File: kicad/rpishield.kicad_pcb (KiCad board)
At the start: 2 copper layers, 64 x 56 mm, 23 parts

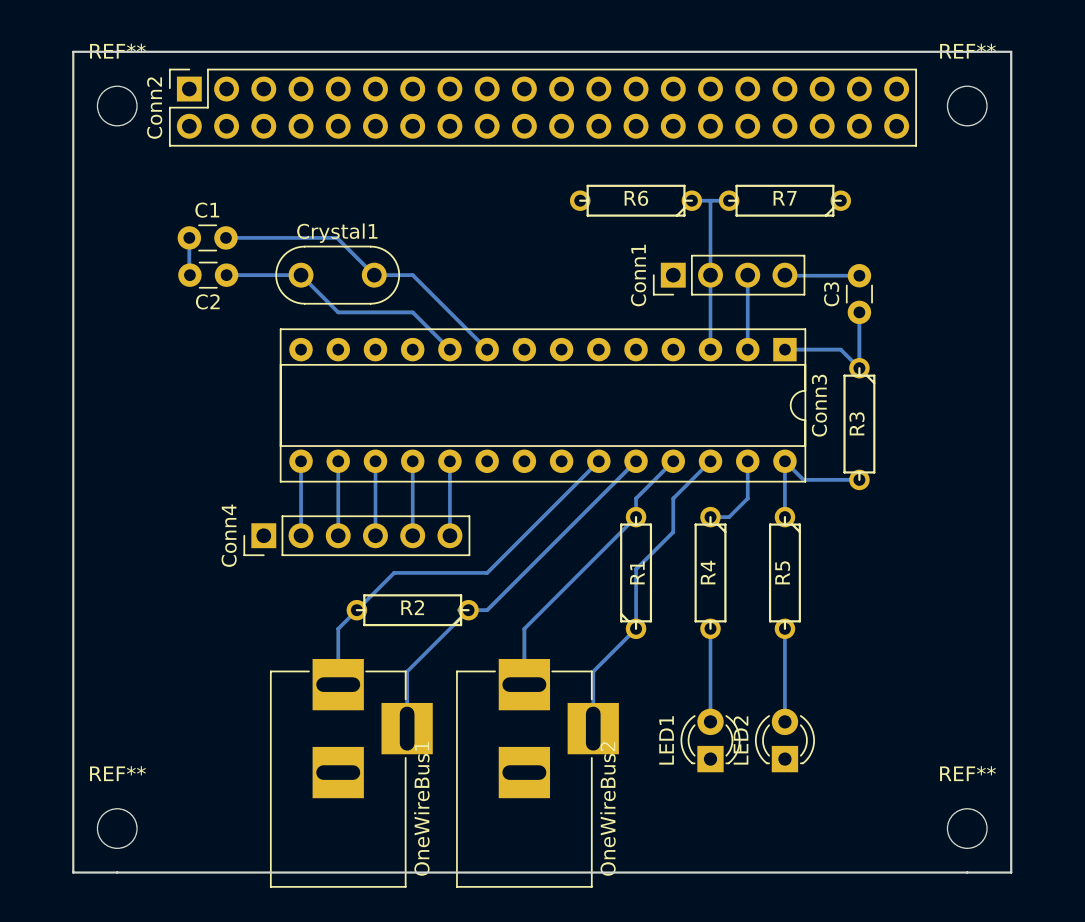
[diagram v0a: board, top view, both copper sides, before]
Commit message: Round corner, via, gnd pour.
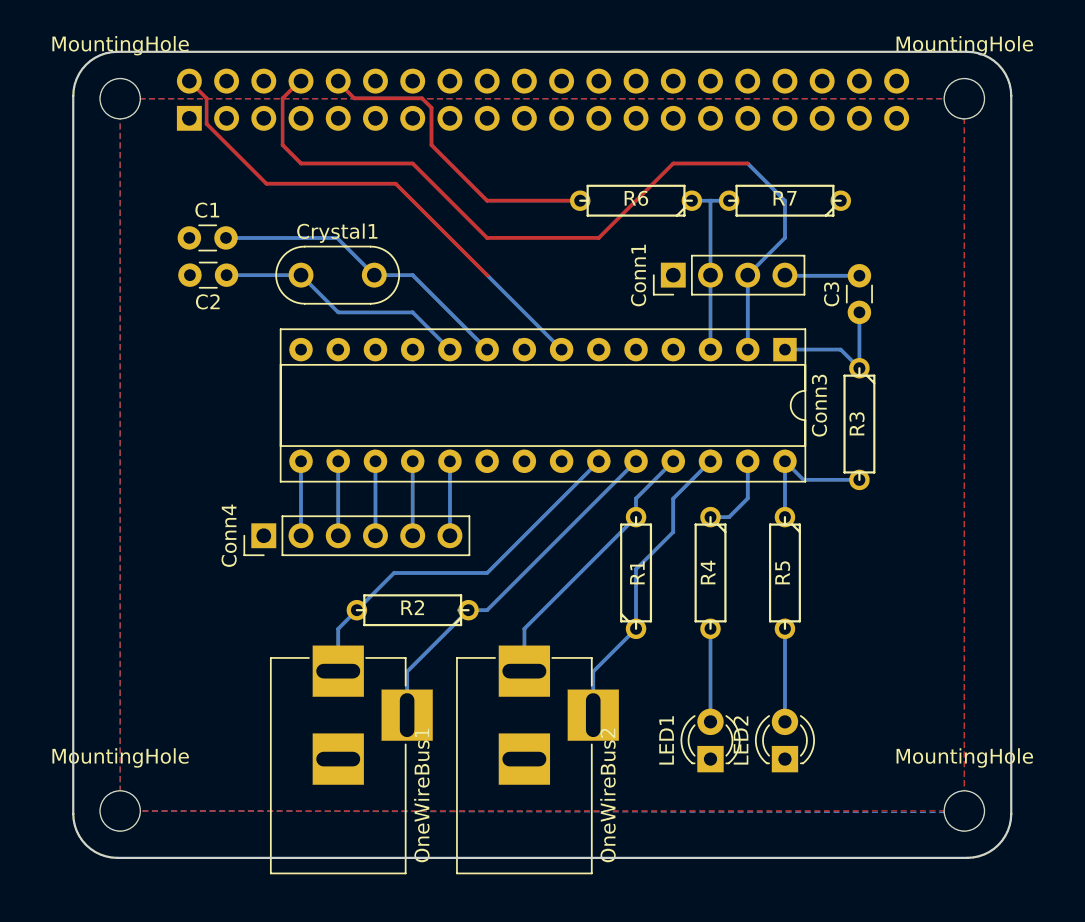
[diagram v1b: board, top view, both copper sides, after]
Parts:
- Conn2: moved to B.Cu
- MountingHole (x4): renamed from REF**; value MountingHole_2.7mm_M2.5 -> MountingHole_2.75mm_M2.5
- moved Conn2 2.00 mm to (121.9, 68.0), turned to 270 degrees
- moved MountingHole 1.22 mm to (117.2, 115.3)
- moved MountingHole 1.22 mm to (174.8, 115.3)
- moved OneWireBus1 0.92 mm to (132.1, 105.8)
- moved OneWireBus2 0.92 mm to (144.8, 105.8)
- moved MountingHole 0.54 mm to (117.2, 66.7)
- moved MountingHole 0.54 mm to (174.8, 66.7)
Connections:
- Conn2 pad 1: /VCC -> Net-(Conn2-Pad1)
- Conn2 pad 10: GND -> /RX_RPI
- Conn2 pad 2: Net-(Conn2-Pad2) -> /VCC
- Conn2 pad 25: Net-(Conn2-Pad25) -> GND
- Conn2 pad 39: Net-(Conn2-Pad39) -> GND
- Conn2 pad 7: /RX -> Net-(Conn2-Pad7)
- Conn2 pad 8: Net-(Conn2-Pad8) -> /RX
- Conn2 pad 9: /RX_RPI -> GND
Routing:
- net /RX: track 5.62 -> 56.7 mm
- net /VCC: track 0.00 -> 34.0 mm
- net /RX_RPI: track 0.00 -> 21.5 mm
- net GND: track 3.28 -> 0.73 mm
- added copper zone on B.Cu, net GND
- added copper zone on F.Cu, net GND
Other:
- board size 64 x 56 mm -> 64 x 55 mm

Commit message: 20x2 pin strip.
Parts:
- Conn2: footprint Socket_Strips:Socket_Strip_Straight_2x20_Pitch2.54mm -> Pin_Headers:Pin_Header_Straight_2x20_Pitch2.54mm; moved to F.Cu
- moved Conn2 0.54 mm to (121.9, 68.6), turned to 90 degrees
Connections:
- net /VCC renamed /VCC_AVR
- Conn2 pad 1: Net-(Conn2-Pad1) -> /VCC_SPI
- Conn2 pad 10: /RX_RPI -> Net-(Conn2-Pad10)
- Conn2 pad 25: GND -> Net-(Conn2-Pad25)
- Conn2 pad 6: Net-(Conn2-Pad6) -> /RX
- Conn2 pad 8: /RX -> /RX_RPI
- Conn3 pad 15: /D9 -> Net-(Conn3-Pad15)
- Conn4 pad 2: /D9 -> /VCC_SPI
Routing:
- net /VCC_SPI: track 0.00 -> 33.2 mm
- net /D9: track 5.08 -> 0.00 mm
- net /RX_RPI: track 21.5 -> 24.4 mm
- net /RX: track 56.7 -> 54.5 mm
- net /VCC_AVR: track 34.0 -> 35.3 mm
- net GND: track 0.73 -> 0.00 mm
- removed copper zone on F.Cu, net GND

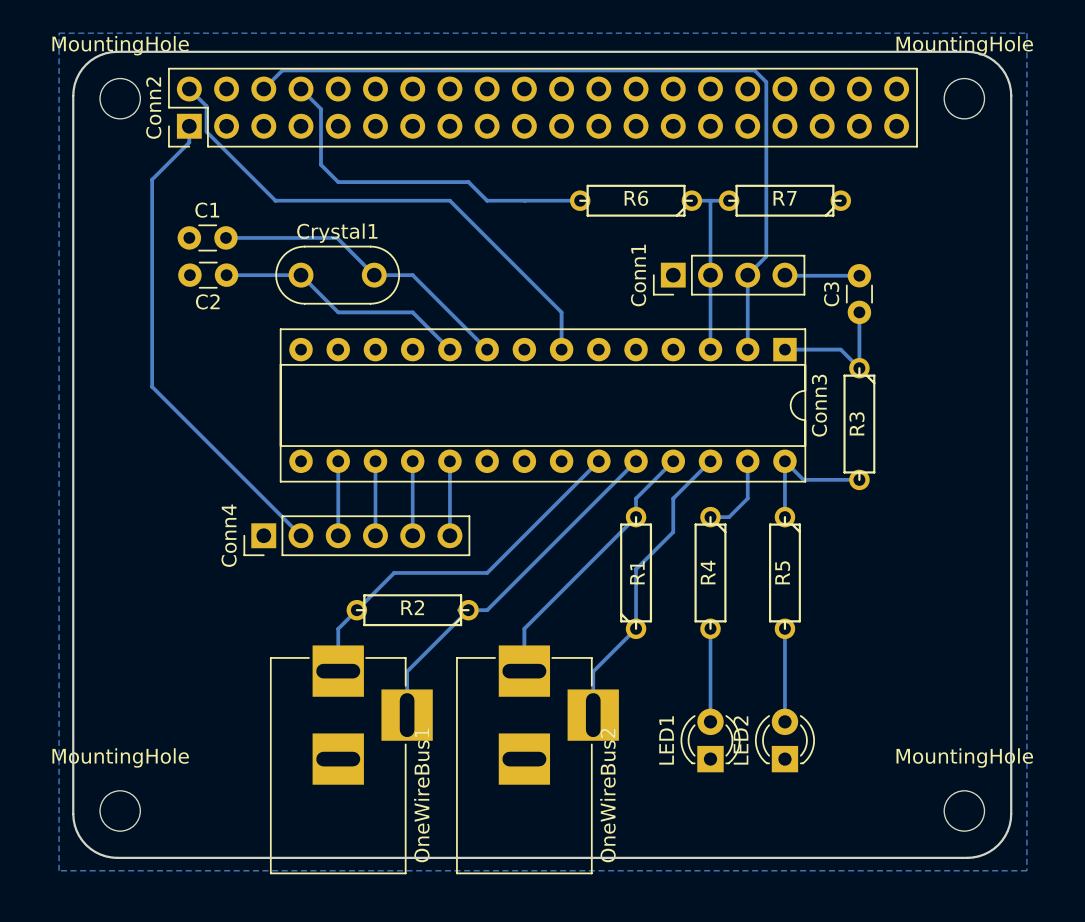
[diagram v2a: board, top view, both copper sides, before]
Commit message: Distance rule, custom header.
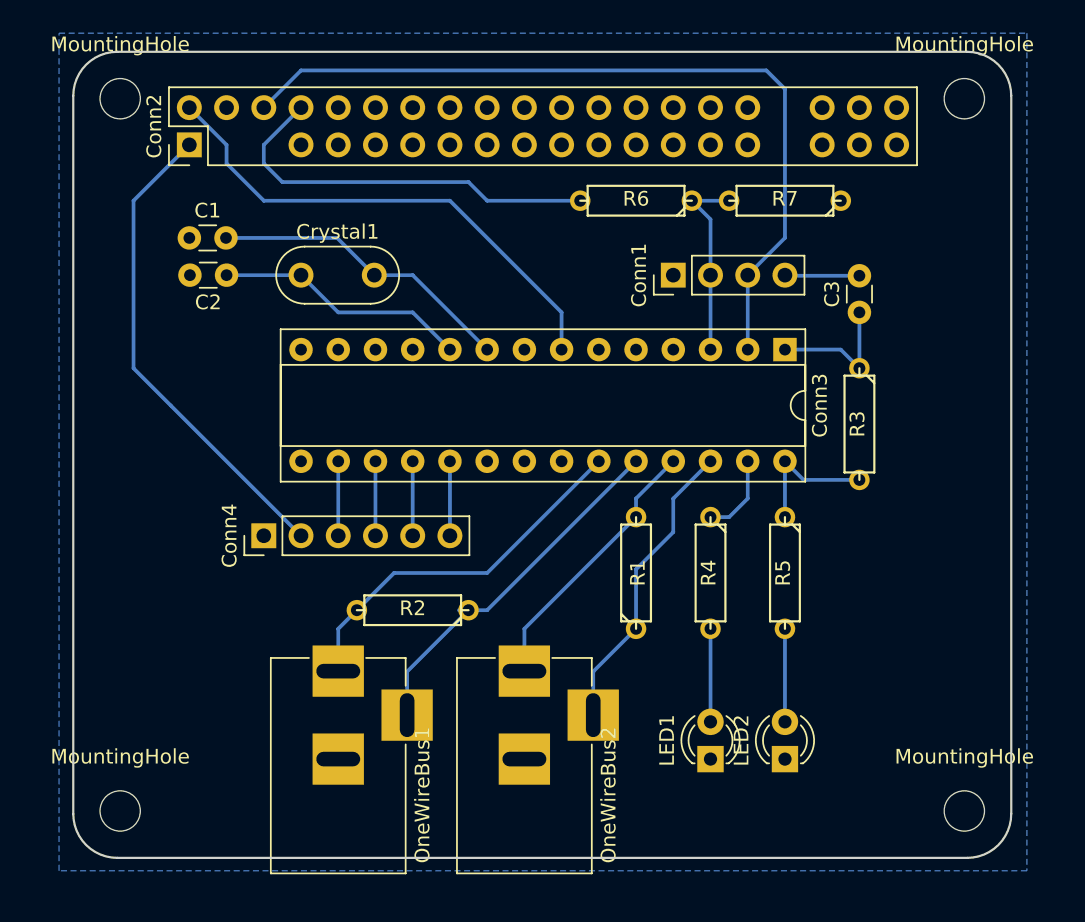
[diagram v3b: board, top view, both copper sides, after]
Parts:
- Conn2: footprint Pin_Headers:Pin_Header_Straight_2x20_Pitch2.54mm -> header220:Custom_Header_2x20_Pitch2.54mm
- moved Conn2 1.27 mm to (121.9, 69.8)
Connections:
- C1 pad 1: GND -> Net-(C1-Pad1)
- C2 pad 2: GND -> Net-(C1-Pad1)
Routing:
- net /RX_RPI: track 24.4 -> 27.5 mm
- net /RX: track 54.5 -> 56.5 mm
- net /VCC_AVR: track 35.3 -> 34.5 mm
- net /TX: track 13.2 -> 13.8 mm
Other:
- net class Default: clearance 0.2 -> 0.3
- rule pad_to_mask_clearance: 0.2 -> 0.3
- rule trace_clearance: 0.2 -> 0.3

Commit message: Ground fill, RPi pinhole, schema lib, cleanup.
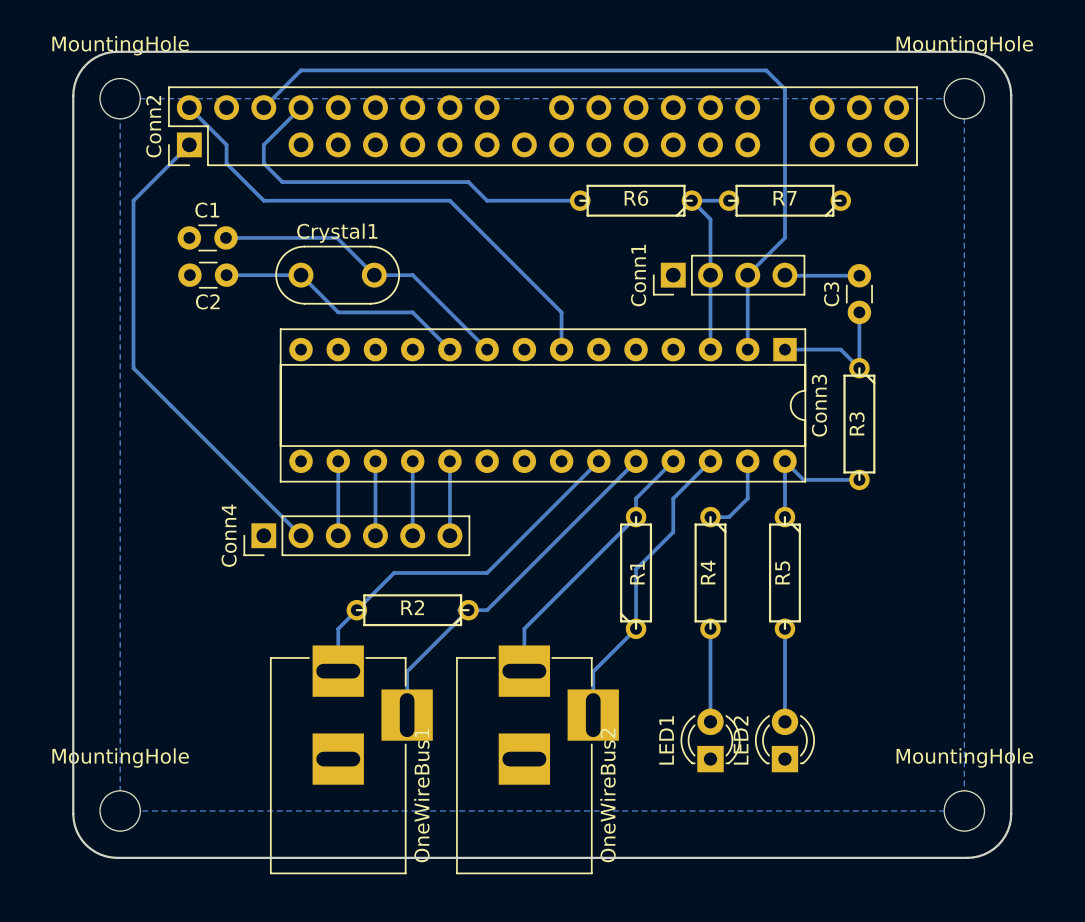
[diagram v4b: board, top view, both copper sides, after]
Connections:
- C1 pad 1: Net-(C1-Pad1) -> GND
- C2 pad 2: Net-(C1-Pad1) -> GND
- Conn2 pad 25: Net-(Conn2-Pad25) -> GND
- Conn2 pad 9: GND -> Net-(Conn2-Pad9)
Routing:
- net /RX: track 56.5 -> 56.0 mm

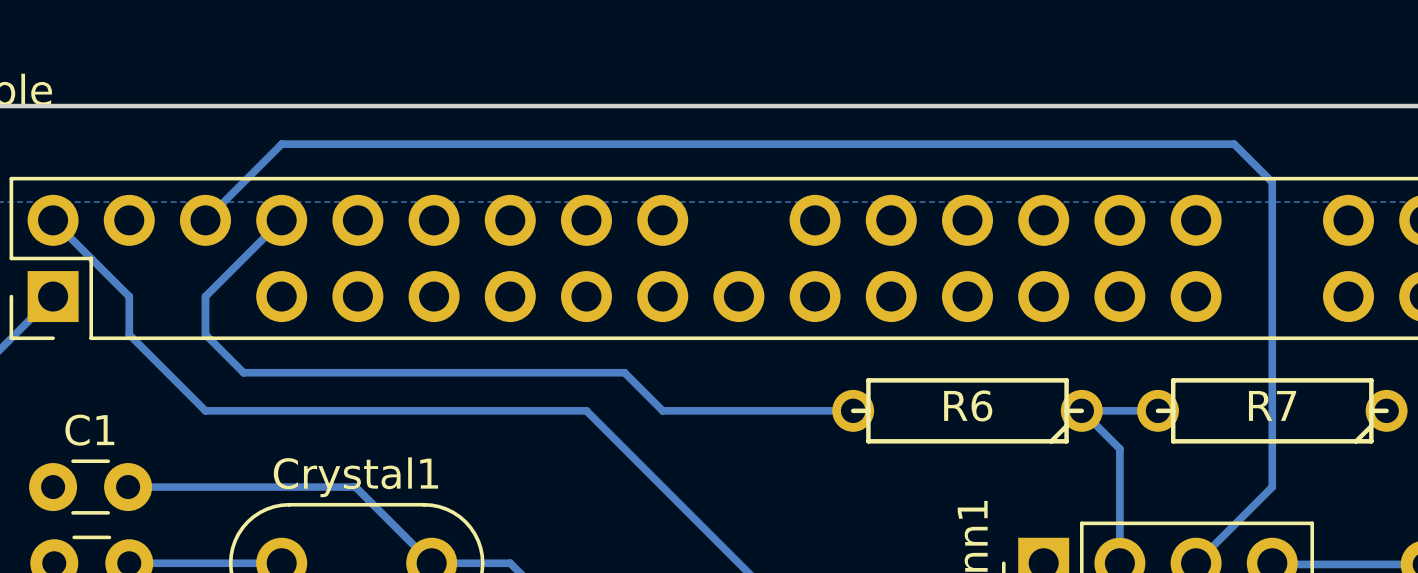
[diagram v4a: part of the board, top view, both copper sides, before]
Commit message: Obsolate models, RX/RT fix.
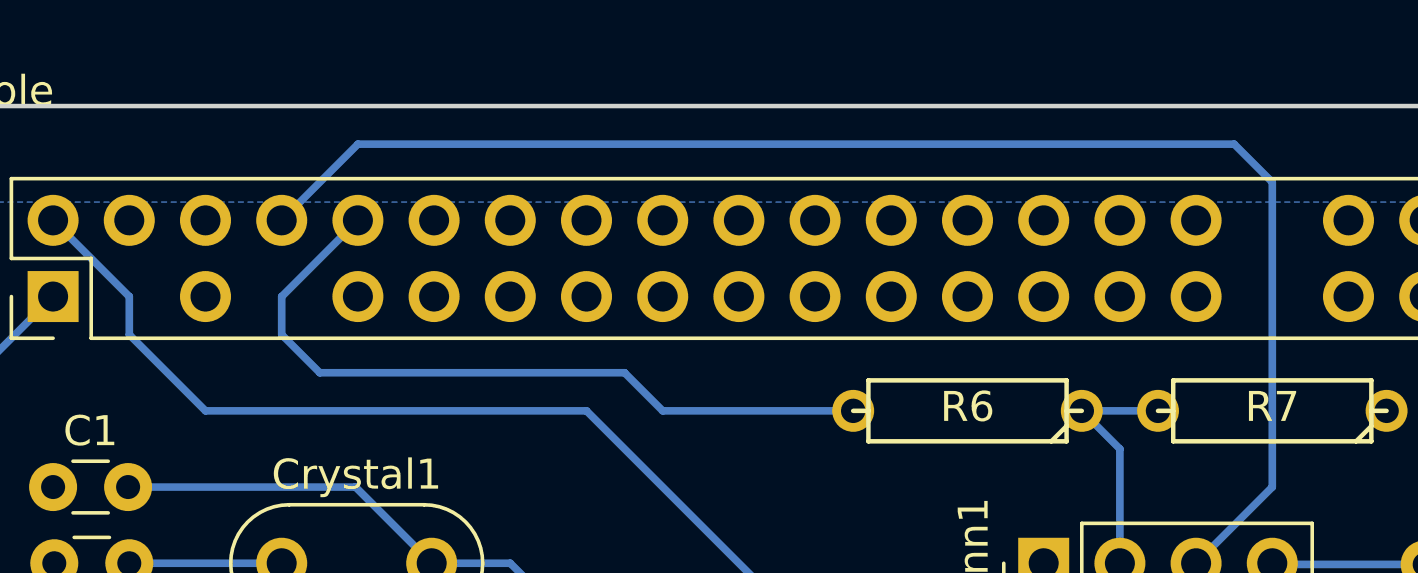
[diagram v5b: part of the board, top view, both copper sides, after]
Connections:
- Conn2 pad 10: Net-(Conn2-Pad10) -> /RX_RPI
- Conn2 pad 6: /RX -> Net-(Conn2-Pad6)
- Conn2 pad 8: /RX_RPI -> /RX
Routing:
- net /RX: track 56.0 -> 53.4 mm
- net /RX_RPI: track 27.5 -> 25.0 mm

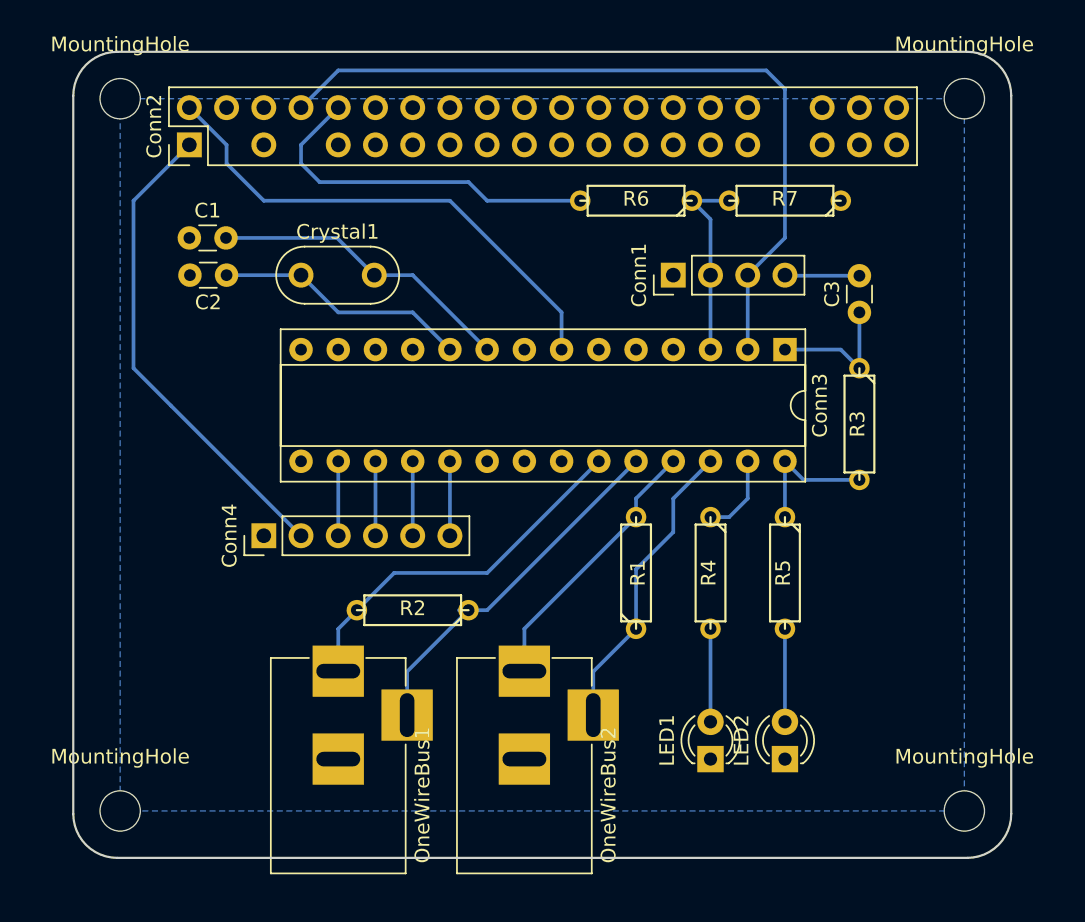
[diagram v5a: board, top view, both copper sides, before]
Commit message: Ground pad, track cleanup.
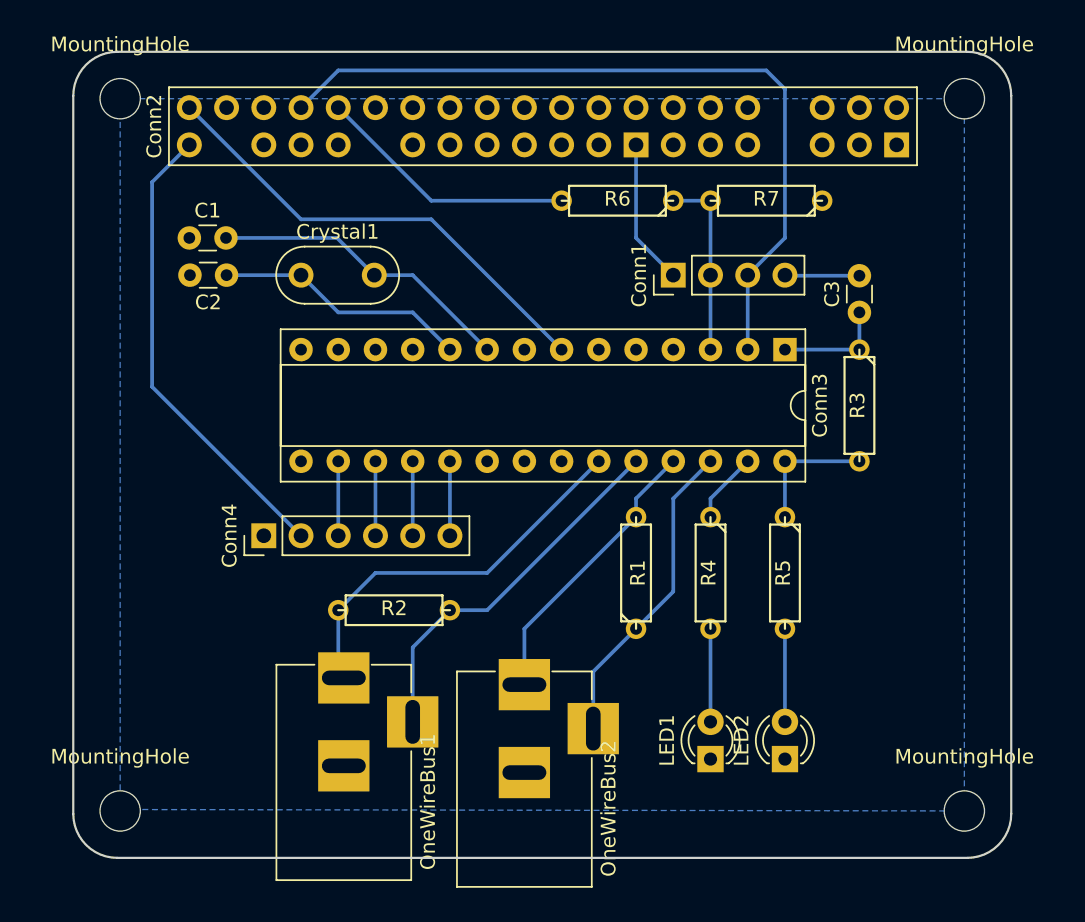
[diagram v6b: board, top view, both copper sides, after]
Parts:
- moved R2 1.27 mm to (135.9, 101.6)
- moved R3 1.27 mm to (167.6, 87.6)
- moved R6 1.27 mm to (151.1, 73.7)
- moved R7 1.27 mm to (161.3, 73.7)
- moved OneWireBus2 0.92 mm to (144.8, 106.7)
- moved OneWireBus1 0.60 mm to (132.5, 106.2)
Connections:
- Conn1 pad 1: GND -> /GND_UART
- Conn2 pad 25: GND -> /GND_UART
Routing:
- net /GND_UART: track 0.00 -> 9.94 mm
- net /RX_RPI: track 25.0 -> 17.9 mm
- net /VCC_AVR: track 34.5 -> 32.2 mm
- net /RST: track 9.68 -> 7.62 mm
- net /A5: track 10.0 -> 8.89 mm
- net /A4: track 5.99 -> 4.86 mm
- net /TX: track 13.8 -> 12.7 mm
- net /VCC_SPI: track 33.0 -> 31.9 mm
- net /A1: track 26.5 -> 25.6 mm
- net /XTAL1: track 21.6 -> 21.0 mm
- net /A2: track 20.0 -> 19.4 mm
